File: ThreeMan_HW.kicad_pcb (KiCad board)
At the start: 2 copper layers, 80 x 40 mm, 76 parts, among them J1 USB4135-GF-A, J2 JST-PH-2mm, J3 TC2030_ICSP, SW1 SW_Push, SW2 SW_SPDT_312, U1 MCP73831T-2ACI/OT, U2 74HC595, U3 ATTINY85-20SUR, U4 TPS7A20, U5 ULQ2003D, U6 ULQ2003D

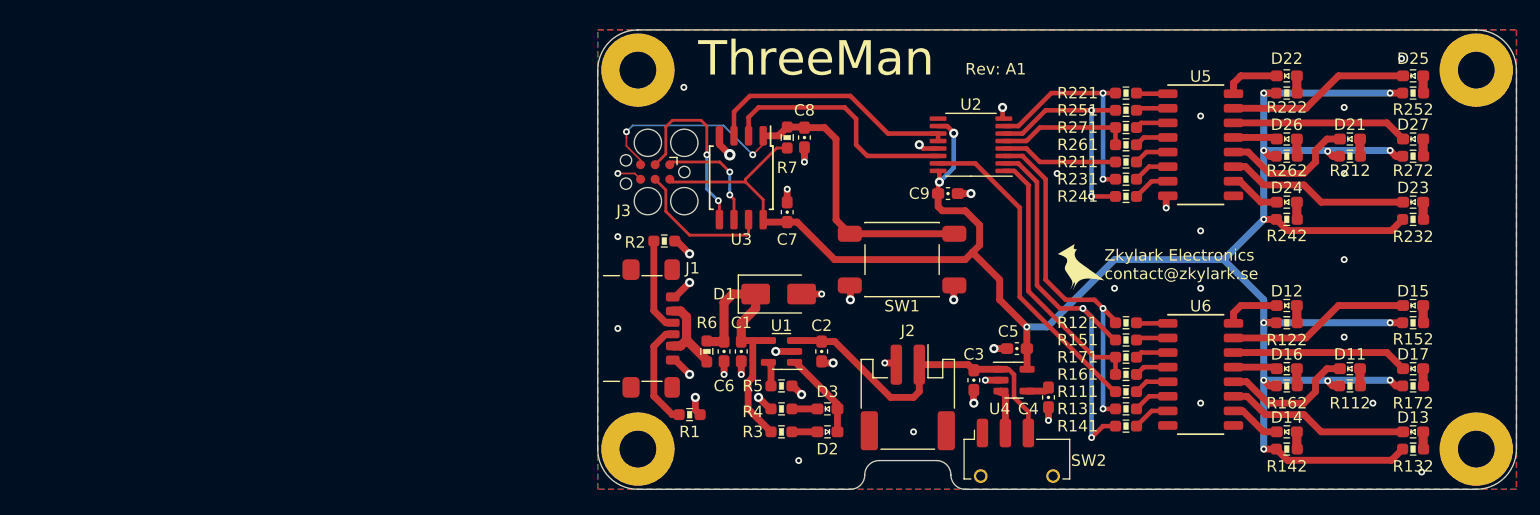
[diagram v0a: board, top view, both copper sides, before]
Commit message: Ported all components to zpklib
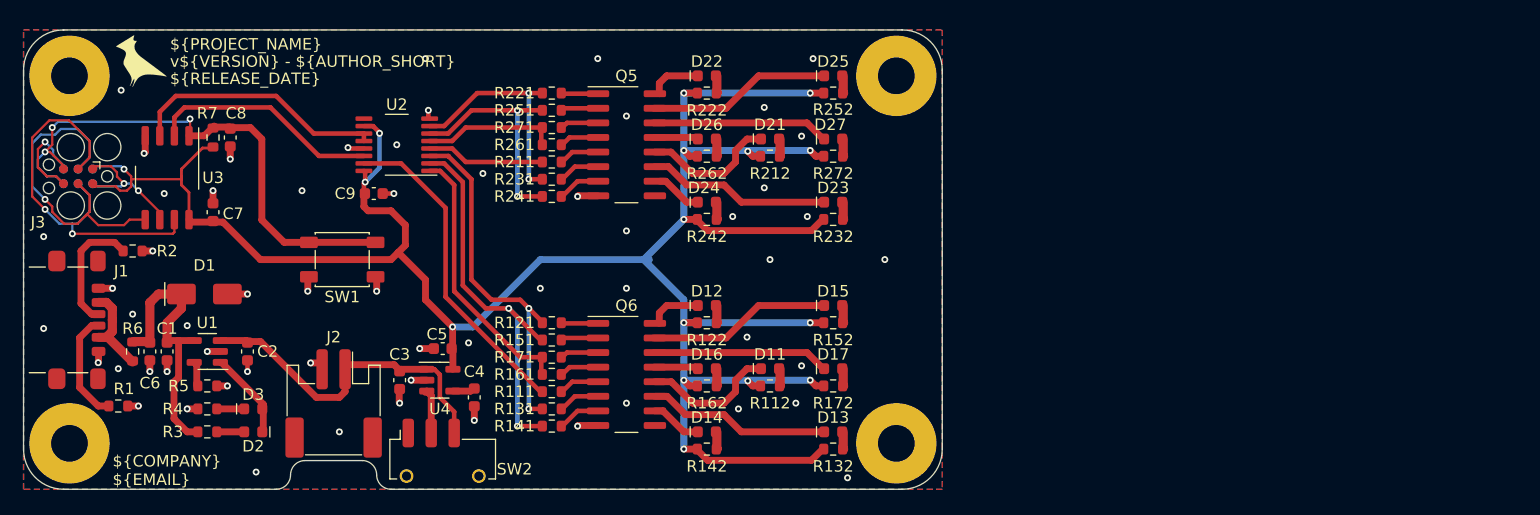
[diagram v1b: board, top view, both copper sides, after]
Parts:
- removed U5, U6: ULQ2003D, Package_SO:SOIC-16-N_3.8x9.8mm_P1.27mm
- added G***: LOGO, logo:Zkylark_logo_5x5mm, F.Cu at (75.2, 62.8)
- added Q5: ULQ2003D, package_SO:SOIC-16_3.9x9.9mm_P1.27mm, F.Cu at (117.5, 70.0)
- added Q6: ULQ2003D, package_SO:SOIC-16_3.9x9.9mm_P1.27mm, F.Cu at (117.5, 90.0)
- C1, C2, C3, C4, C5, C6, C7, C8, C9: footprint Capacitor_SMD:C_0603_HS -> capacitor:C_0603_1608Metric
- D1: value SMAJ5.0A -> 9.2V; footprint Diode_SMD:DO-214AC -> diode:D_SMA
- D11, D12, D13, D14, D15, D16, D17, D2, D21, D22, D23, D24, D25, D26, D27: value Red -> LTST-C191KRKT; footprint LED_SMD:LED_0603_HS -> led:LED_0603_1608Metric
- D3: value Green -> LTST-C190KGKT[A; footprint LED_SMD:LED_0603_HS -> led:LED_0603_1608Metric
- H1, H2, H3, H4: value M3 -> MountingHole_Pad; footprint MountingHole:MountingHole_3.2mm_M3_Pad -> mounting_hole:MountingHole_3.2mm_Pad
- J1: footprint Connector_USB:USB4135-GF-A -> connector_usb:GCT-USB4135-GF-A
- J2: value JST-PH-2mm -> S2B-PH; footprint Connector_JST:JST_PH_S2B-PH-SM4-TB_1x02-1MP_P2.00mm_Horizontal -> connector_jst:JST_PH_B2B-PH-SM4-TB_1x02-1MP_P2.00mm_Vertical
- J3: value TC2030_ICSP -> TC2030; footprint Connector:Tag-Connect_TC2030-IDC-FP_2x03_P1.27mm_Vertical -> connector_tagconnect:TagConnect_TC2030_2x3_DualSide
- R1, R111, R112, R121, R122, R131, R132, R141, R142, R151, R152, R161, R162, R171, R172, R2, R211, R212, R221, R222, R231, R232, R241, R242, R251, R252, R261, R262, R271, R272, R3, R4, R5, R6, R7: footprint Resistor_SMD:R_0603_HS -> resistor:R_0603_1608Metric
- SW1: value SW_Push -> PTS647; footprint Switch_Button_SMD:SW_SPST_TS04-66-95-BK-160-SMT -> switch:SW_Push_SPST_4.5x4.5mm_H7.0mm
- SW2: value SW_SPDT_312 -> CSS-1210TB; footprint Switch_Slide_SMD:CSS-1210TB -> switch:CSS-1210TB
- U1: value MCP73831T-2ACI/OT -> MCP73831; footprint Package_TO_SOT_SMD:SOT-23-5 -> package_TO_SOT:SOT-23-5
- U2: footprint Package_SO:TSSOP-16_4.4x5mm_P0.65mm -> package_SO:TSSOP-16_4.4x5mm_P0.65mm
- U3: value ATTINY85-20SUR -> ATTINY85; footprint Package_SO:SOIC-8_5.3x5.3mm_P1.27mm -> package_SO:SOIC-8_5.3x5.3mm_P1.27mm
- U4: footprint Package_TO_SOT_SMD:SOT-23-5 -> package_TO_SOT:SOT-23-5
- moved H2 50.5 mm to (141.0, 64.0)
- moved H4 50.5 mm to (141.0, 96.0)
- moved D11 50.5 mm to (130.0, 89.5)
- moved D12 50.5 mm to (124.5, 84.0)
- moved D13 50.5 mm to (135.5, 95.0)
- moved D14 50.5 mm to (124.5, 95.0)
- moved D15 50.5 mm to (135.5, 84.0)
- moved D16 50.5 mm to (124.5, 89.5)
- moved D17 50.5 mm to (135.5, 89.5)
- moved D21 50.5 mm to (130.0, 69.5)
- moved D22 50.5 mm to (124.5, 64.0)
- moved D23 50.5 mm to (135.5, 75.0)
- moved D24 50.5 mm to (124.5, 75.0)
- moved D25 50.5 mm to (135.5, 64.0)
- moved D26 50.5 mm to (124.5, 69.5)
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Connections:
- net 3V3 renamed /3V3
- net GND renamed /GND
- J3 pad 3: /MOSI -> /SCK
- J3 pad 4: /SCK -> /MOSI
- R112 pad 1: Net-(D11-A) -> Net-(D11-PadA)
- R122 pad 1: Net-(D12-A) -> Net-(D12-PadA)
- R132 pad 1: Net-(D13-A) -> Net-(D13-PadA)
- R142 pad 1: Net-(D14-A) -> Net-(D14-PadA)
- R152 pad 1: Net-(D15-A) -> Net-(D15-PadA)
- R162 pad 1: Net-(D16-A) -> Net-(D16-PadA)
- R172 pad 1: Net-(D17-A) -> Net-(D17-PadA)
- R212 pad 1: Net-(D21-A) -> Net-(D21-PadA)
- R222 pad 1: Net-(D22-A) -> Net-(D22-PadA)
- R232 pad 1: Net-(D23-A) -> Net-(D23-PadA)
- R242 pad 1: Net-(D24-A) -> Net-(D24-PadA)
- R252 pad 1: Net-(D25-A) -> Net-(D25-PadA)
- R262 pad 1: Net-(D26-A) -> Net-(D26-PadA)
- R272 pad 1: Net-(D27-A) -> Net-(D27-PadA)
- R3 pad 2: Net-(D2-A) -> Net-(D2-PadA)
- R4 pad 2: Net-(D3-K) -> Net-(D3-PadC)
- U1 pad 1: Net-(D2-K) -> Net-(U1-STAT)
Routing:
- net /SCK: track 12.5 -> 34.5 mm, vias 0 -> 2
- net Net-(D23-K): track 16.0 -> 0.00 mm
- net Net-(D13-K): track 16.0 -> 0.00 mm
- net Net-(Q6-C2): track 0.00 -> 15.9 mm
- net Net-(Q5-C2): track 0.00 -> 15.9 mm
- net Net-(D25-K): track 15.9 -> 0.00 mm
- net Net-(D15-K): track 15.9 -> 0.00 mm
- net Net-(Q6-C6): track 0.00 -> 15.9 mm
- net Net-(Q5-C6): track 0.00 -> 15.9 mm
- net Net-(Q6-C3): track 0.00 -> 15.3 mm
- net Net-(Q5-C3): track 0.00 -> 15.3 mm
- net Net-(D27-K): track 15.3 -> 0.00 mm
- net Net-(D17-K): track 15.3 -> 0.00 mm
- net Net-(D21-K): track 11.9 -> 0.00 mm
- net Net-(D11-K): track 11.9 -> 0.00 mm
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- added copper zone on In1.Cu, net /GND
- added copper zone on In2.Cu, net /GND
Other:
- copper layers 2 -> 4
- board text added: "${COMPANY} ${EMAIL}"
- board text added: "${PROJECT_NAME}"
- board text added: "${RELEASE_DATE}"
- board text added: "Die"
- board text added: "Face"
- board text added: "v${VERSION} - ${AUTHOR_SHORT}"
- board text removed: "${COMPANY} ${COMMENT1}"
- board text removed: "${TITLE}"
- board text removed: "Rev: ${REVISION}"

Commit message: Added JLCPCB PCB ordering information to PCB.Comments
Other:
- board text added: "${LAYER}"
